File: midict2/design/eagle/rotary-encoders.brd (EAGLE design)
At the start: 100 x 74.9 mm, 55 parts, among them U1 SN74HC165DR, U2 SN74HC165DR, U3 SN74HC165DR

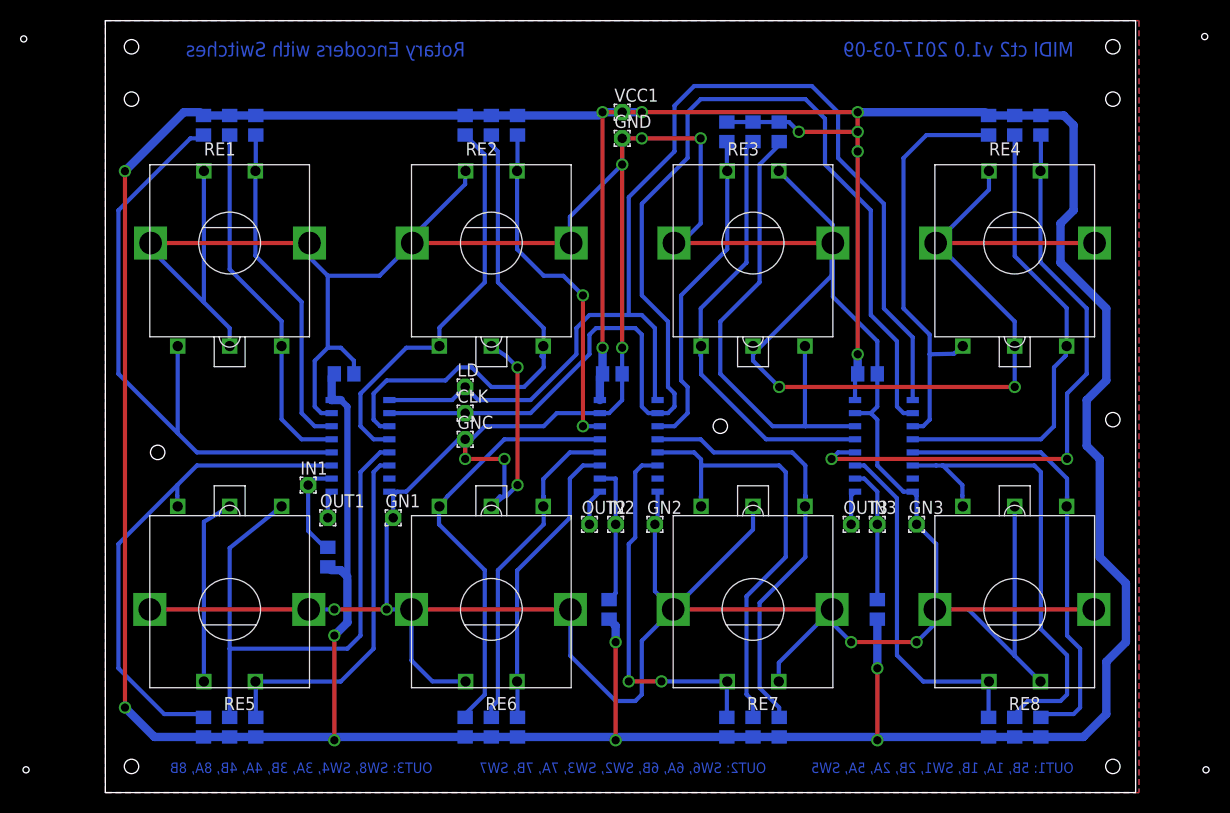
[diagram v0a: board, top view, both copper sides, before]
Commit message: midict2 rotary encoders build and verified
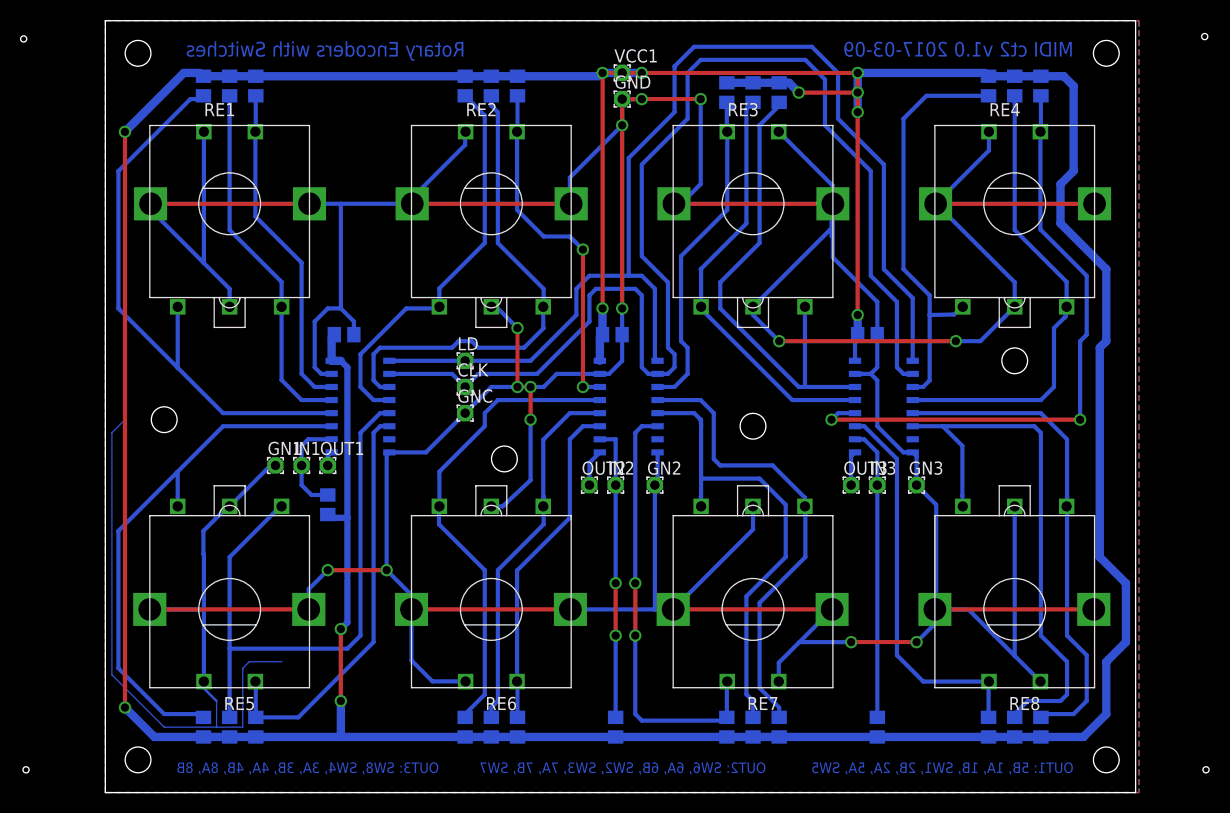
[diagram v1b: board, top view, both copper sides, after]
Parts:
- moved GN1 12.5 mm to (16.5, 31.8)
- moved R18 11.4 mm to (49.5, 6.35)
- moved R19 11.4 mm to (74.9, 6.35)
- moved R17 5.08 mm to (21.6, 27.9)
- moved OUT1 5.08 mm to (21.6, 31.8)
- moved C1 3.81 mm to (23.2, 44.5)
- moved C2 3.81 mm to (49.2, 44.5)
- moved C3 3.81 mm to (74.0, 44.5)
- moved GND 3.81 mm to (50.2, 67.3)
- moved R10 3.81 mm to (90.8, 68.6)
- moved R13 3.81 mm to (85.7, 68.6)
- moved R14 3.81 mm to (88.3, 68.6)
- moved R21 3.81 mm to (9.53, 68.6)
- moved R22 3.81 mm to (12.1, 68.6)
- moved R23 3.81 mm to (14.6, 68.6)
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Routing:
- net GND: track 584.2 -> 634.0 mm
- net IN3: track 13.2 -> 28.4 mm
- net VCC: track 448.0 -> 433.0 mm, vias 16 -> 12
- net IN2: track 13.5 -> 28.5 mm, vias 0 -> 2
- net RE8B: track 46.3 -> 53.9 mm
- net SW7: track 36.1 -> 42.5 mm
- net SW5: track 35.2 -> 40.1 mm
- net RE8A: track 44.9 -> 49.2 mm
- net RE6B: track 41.5 -> 45.7 mm
- net RE2B: track 51.3 -> 47.1 mm
- net RE1A: track 59.5 -> 55.4 mm
- net SW8: track 34.1 -> 37.9 mm
- net SW6: track 28.8 -> 32.6 mm
- net RE6A: track 33.7 -> 37.5 mm
- net RE5B: track 48.2 -> 51.8 mm
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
